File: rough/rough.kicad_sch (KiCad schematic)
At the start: 4 parts, among them J1 250-202 Wago, J2 5788336-1 TE USB-B, J3 484090003 Molex 2x USB-A v3, J4 TMJD0012BENL Tagolas Ethernet

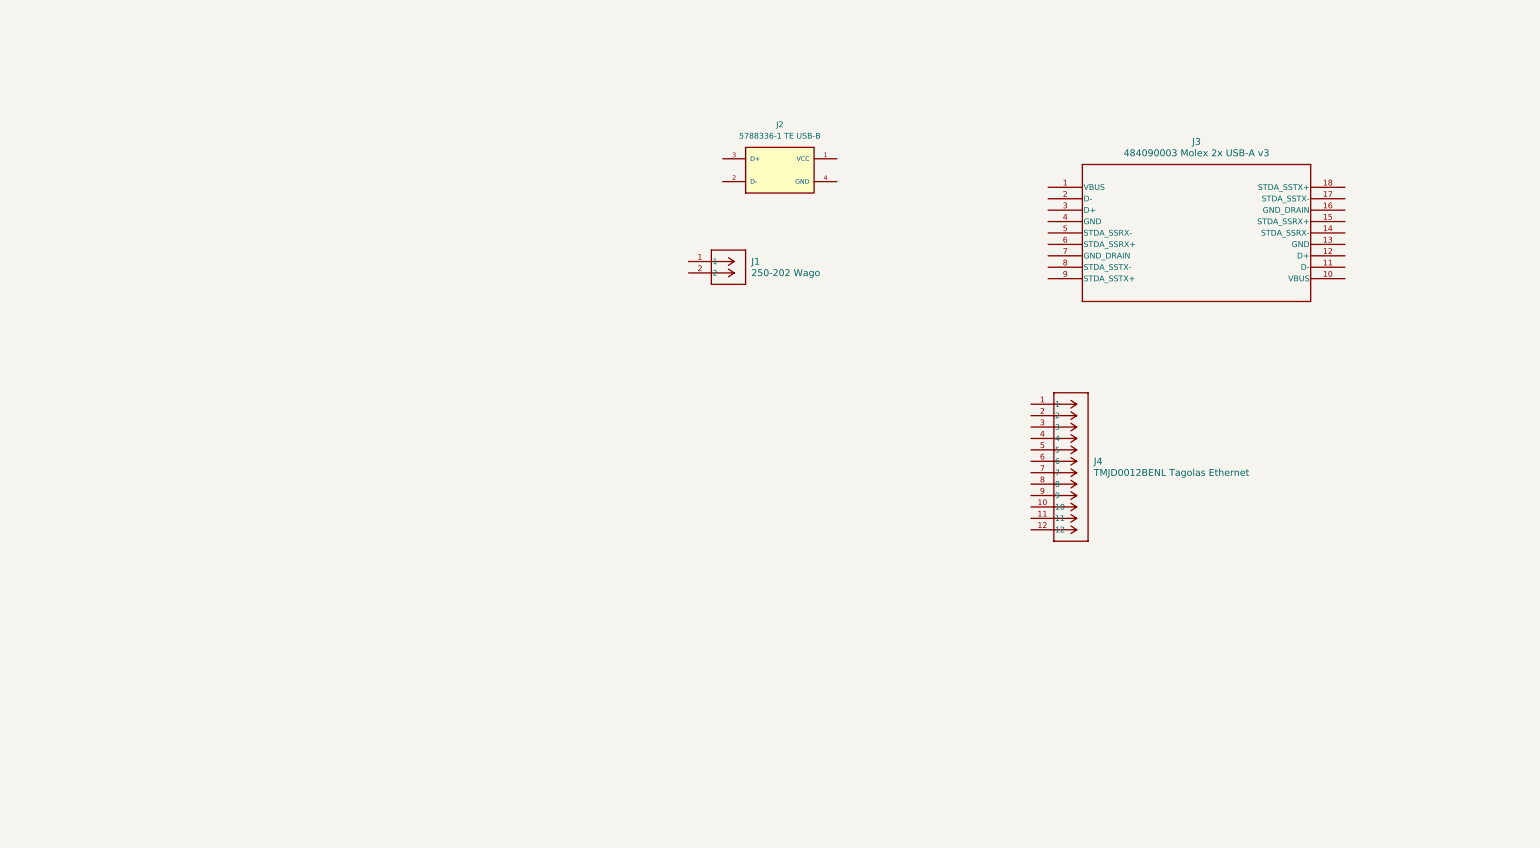
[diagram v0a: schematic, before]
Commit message: Break libs by MFG
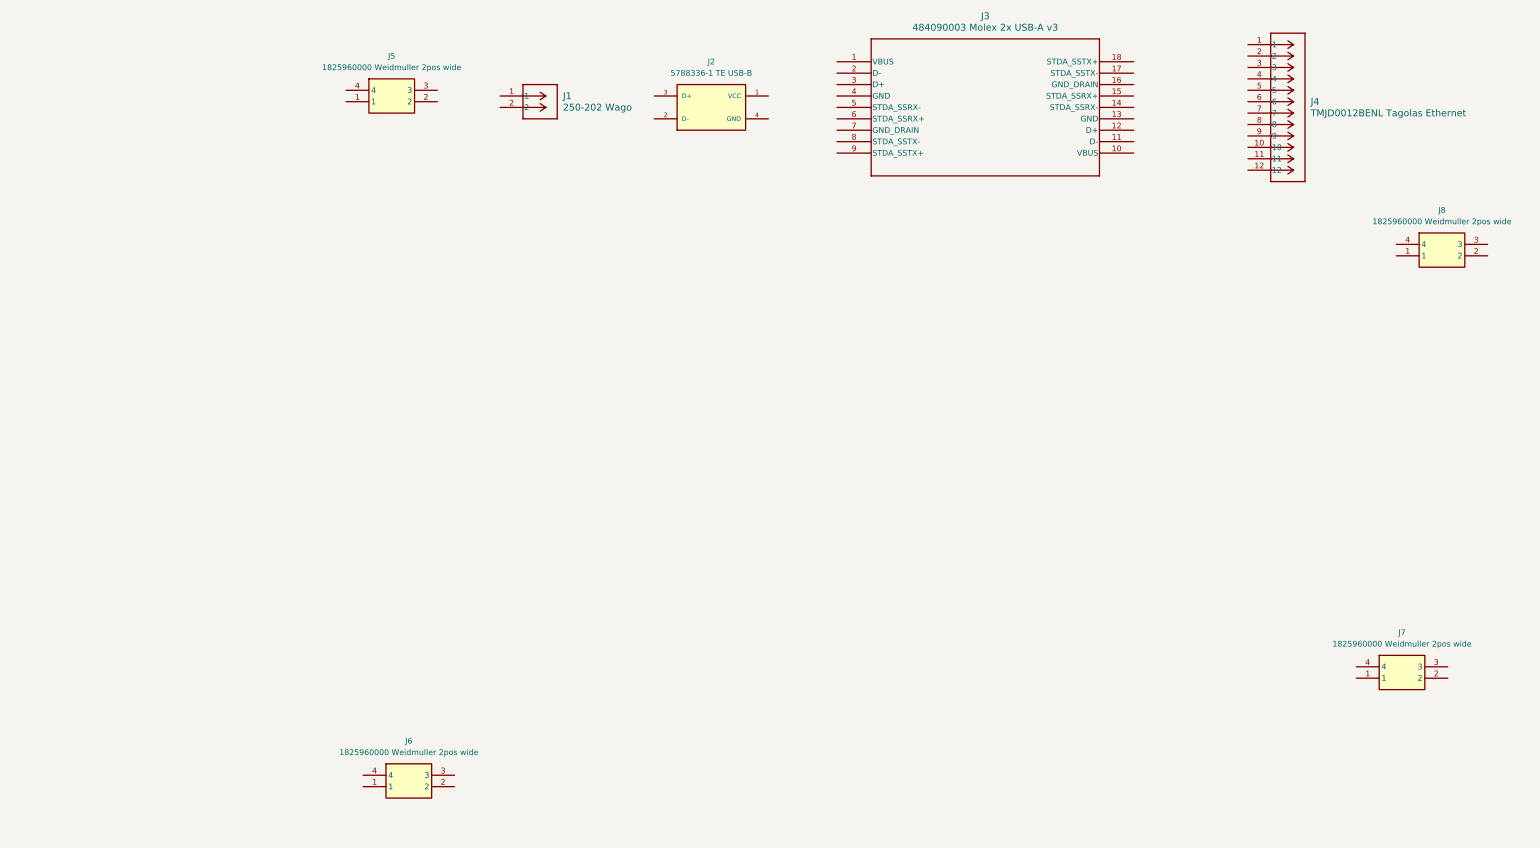
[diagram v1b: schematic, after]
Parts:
- added J5, J6, J7, J8: 1825960000 Weidmuller 2pos wide, Weidmuller:CONN_1825960000 2pos Wide, symbol Snapeda:1825960000 Weidmuller 2pos wide
- J1: footprint SnapEDA:CONN_250-202_WAG -> Wago:CONN_250-202
- J2: footprint SnapEDA:TE_5788336-1 -> TE:TE_5788336-1_USB-B
- J3: footprint SnapEDA:48409-0003_MOL -> Molex:48409-0003_MOL
- J4: footprint SnapEDA:CONN12_0012BENL_TAL -> Taoglas:CONN12_0012BENL_TAL
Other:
- moved on the sheet: J1, J2, J3, J4

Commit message: Playing with weidmuller
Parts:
- added J10, J11, J9: 1826000000 6pos wide, Weidmuller:1826000000, symbol Weidmuller:1826000000 6pos wide
- added J12, J13, J14, J15, J16, J17: 1825970000 3pos wide, Weidmuller:1825970000, symbol Weidmuller:1825970000 3pos wide
- J5, J6, J7, J8: footprint Weidmuller:CONN_1825960000 2pos Wide -> Weidmuller:1825960000
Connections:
- new net +5V: J10.1, J10.10, J10.11, J10.12, J10.2, J10.3, J10.4, J10.5, J10.6, J10.7, J10.8, J10.9
- new net GND: J9.1, J9.10, J9.11, J9.12, J9.2, J9.3, J9.4, J9.5, J9.6, J9.7, J9.8, J9.9

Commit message: wip
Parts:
- added J18: Conn_01x03, symbol Connector_Generic:Conn_01x03
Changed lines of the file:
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@@
+    )
+  )
+  (symbol (lib_id "Connector_Generic:Conn_01x03") (at 88.9 115.57 0) (unit 1)
+    (in_bom yes) (on_board yes) (dnp no) (fields_autoplaced)
+    (property "Reference" "J18" (at 91.44 114.3 0)
+      (effects (font (size 1.27 1.27)) (justify left))
+    )
+    (property "Value" "Conn_01x03" (at 91.44 116.84 0)
+      (effects (font (size 1.27 1.27)) (justify left))
+    )
+    (property "Footprint" "" (at 88.9 115.57 0)
+      (effects (font (size 1.27 1.27)) hide)
+    )
+    (property "Datasheet" "~" (at 88.9 115.57 0)
+      (effects (font (size 1.27 1.27)) hide)
+    )
+    (pin "2")
+    (pin "3")
+    (pin "1")
+    (instances
+      (project "rough"
+        (path "/f58df7cb-3041-45f9-8c3b-f4807dfacb2e"
+          (reference "J18") (unit 1)
+        )
+      )
     )
   )
